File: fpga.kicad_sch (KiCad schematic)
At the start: 57 parts, among them J7 2X05, Q6 2N7002, U11 LIFCL-40-9BG256C, U17 SC18IS602BIPW, U18 W25Q32JVSSIQ, Y2 OSC40M-3.3_S5

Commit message: Created loclib
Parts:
- R58, R65: footprint antmicro-footprints:0603-res -> crosslink-nx-video-converter-footprints:0603-res; symbol antmicroResistors0603:R_0R_0603 -> crosslink-nx-video-converter:R_0R_0603
- U11: footprint antmicro-footprints:BGA-256_16x16_14.0x14.0mm -> crosslink-nx-video-converter-footprints:BGA-256_16x16_14.0x14.0mm; symbol antmicroBGAchips:LIFCL-40-9BG256C -> crosslink-nx-video-converter:LIFCL-40-9BG256C

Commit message: Added revision and title to the schematic sheets
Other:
- title: (none) -> CrossLink-NX Video Converter
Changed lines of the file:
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@@
 (kicad_sch (version 20211123) (generator eeschema)
   (paper "A3")
+  (title_block
+    (title "CrossLink-NX Video Converter")
+    (date "2022-10-27")
+    (rev "1.0.0")
+    (comment 1 "www.antmicro.com")
+    (comment 2 "Antmicro Ltd.")
+  )
   (junction (at 336.55 39.37) (diameter 0) (color 0 0 0 0)
   )

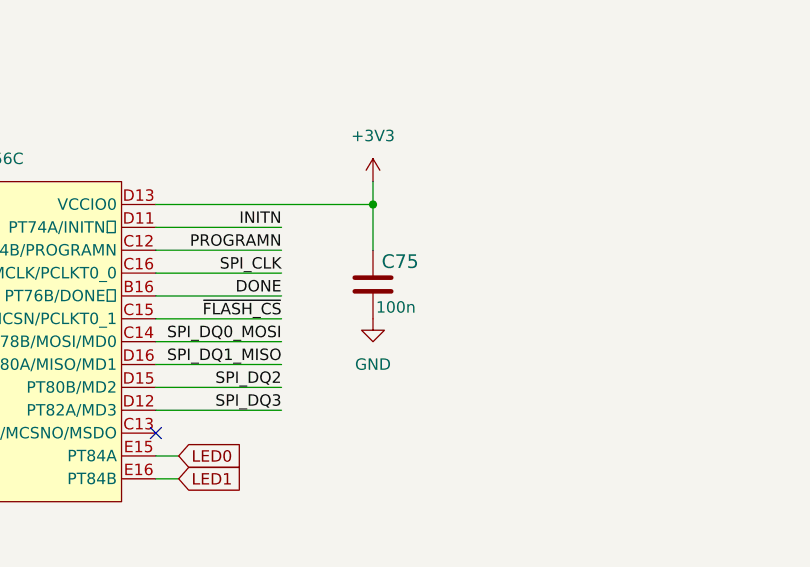
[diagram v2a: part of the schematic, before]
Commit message: Update PCB routing
- apply new DRC
- add FPGA package delay to the high speed traces tunning
- improve GND and power planes
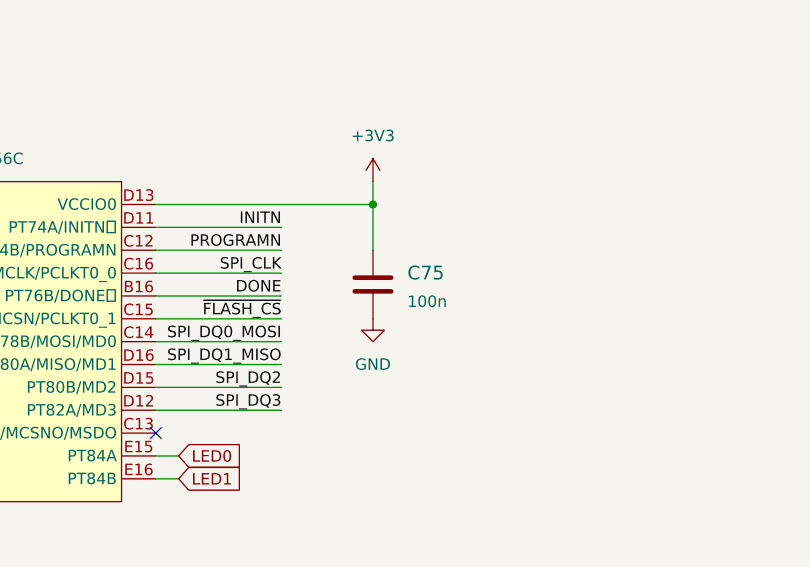
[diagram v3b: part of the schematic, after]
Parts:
- removed C75: C_100n_0402, crosslink-nx-video-converter-footprints:0402-cap, symbol crosslink-nx-video-converter:C_100n_0402
- added C75: C_100n_0201, crosslink-nx-video-converter-footprints:0201-res, symbol crosslink-nx-video-converter:C_100n_0201
- U11: footprint crosslink-nx-video-converter-footprints:BGA-256_16x16_14.0x14.0mm -> crosslink-nx-video-converter-footprints:CrosslinkNX-BGA-256_16x16_14.0x14.0mm
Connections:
- net +3V3: now also C75.1
- net GND: now also C75.2

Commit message: Update project naming convention
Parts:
- C75: footprint crosslink-nx-video-converter-footprints:0201-res -> sdi-mipi-cross-converter-footprints:0201-res; symbol crosslink-nx-video-converter:C_100n_0201 -> sdi-mipi-cross-converter:C_100n_0201
- C79, C80, C81, C82: footprint crosslink-nx-video-converter-footprints:0402-cap -> sdi-mipi-cross-converter-footprints:0402-cap; symbol crosslink-nx-video-converter:C_100n_0402 -> sdi-mipi-cross-converter:C_100n_0402
- D5: footprint crosslink-nx-video-converter-footprints:LED_0603 -> sdi-mipi-cross-converter-footprints:LED_0603; symbol crosslink-nx-video-converter:LTST-C190GKT -> sdi-mipi-cross-converter:LTST-C190GKT
- D6: footprint crosslink-nx-video-converter-footprints:LED_0603 -> sdi-mipi-cross-converter-footprints:LED_0603; symbol crosslink-nx-video-converter:LTST-C190KRKT -> sdi-mipi-cross-converter:LTST-C190KRKT
- J7: footprint crosslink-nx-video-converter-footprints:SHF-105-01-X-D-SM -> sdi-mipi-cross-converter-footprints:SHF-105-01-X-D-SM; symbol crosslink-nx-video-converter:2X05 -> sdi-mipi-cross-converter:2X05
- Q6: footprint crosslink-nx-video-converter-footprints:SOT-23-3 -> sdi-mipi-cross-converter-footprints:SOT-23-3; symbol crosslink-nx-video-converter:2N7002 -> sdi-mipi-cross-converter:2N7002
- R131, R132, R39, R66, R67, R69, R71, R75, R76, R77, R78, R80, R82, R85, R86, R88, R92, R94, R95, R96: footprint crosslink-nx-video-converter-footprints:0402-res -> sdi-mipi-cross-converter-footprints:0402-res; symbol crosslink-nx-video-converter:R_0R_0402 -> sdi-mipi-cross-converter:R_0R_0402
- R58, R65: footprint crosslink-nx-video-converter-footprints:0603-res -> sdi-mipi-cross-converter-footprints:0603-res; symbol crosslink-nx-video-converter:R_0R_0603 -> sdi-mipi-cross-converter:R_0R_0603
- R68, R81, R91, R97: footprint crosslink-nx-video-converter-footprints:0402-res -> sdi-mipi-cross-converter-footprints:0402-res; symbol crosslink-nx-video-converter:R_10k_0402 -> sdi-mipi-cross-converter:R_10k_0402
- R70, R72, R84: footprint crosslink-nx-video-converter-footprints:0402-res -> sdi-mipi-cross-converter-footprints:0402-res; symbol crosslink-nx-video-converter:R_100R_0402 -> sdi-mipi-cross-converter:R_100R_0402
- R79: footprint crosslink-nx-video-converter-footprints:0402-res -> sdi-mipi-cross-converter-footprints:0402-res; symbol crosslink-nx-video-converter:R_1k_0402 -> sdi-mipi-cross-converter:R_1k_0402
- R83, R87, R90: footprint crosslink-nx-video-converter-footprints:0402-res -> sdi-mipi-cross-converter-footprints:0402-res; symbol crosslink-nx-video-converter:R_4k7_0402 -> sdi-mipi-cross-converter:R_4k7_0402
- R89, R93: footprint crosslink-nx-video-converter-footprints:0402-res -> sdi-mipi-cross-converter-footprints:0402-res; symbol crosslink-nx-video-converter:R_2k2_0402 -> sdi-mipi-cross-converter:R_2k2_0402
- S1: footprint crosslink-nx-video-converter-footprints:B3U-3000P -> sdi-mipi-cross-converter-footprints:B3U-3000P; symbol crosslink-nx-video-converter:B3U-3000PM -> sdi-mipi-cross-converter:B3U-3000PM
- TP15, TP16, TP17, TP18, TP19, TP20, TP21, TP22: footprint crosslink-nx-video-converter-footprints:Testpoint_smd_0_75mm -> sdi-mipi-cross-converter-footprints:Testpoint_smd_0_75mm; symbol crosslink-nx-video-converter:TP_SMD_0_75MM -> sdi-mipi-cross-converter:TP_SMD_0_75MM
- U11: footprint crosslink-nx-video-converter-footprints:CrosslinkNX-BGA-256_16x16_14.0x14.0mm -> sdi-mipi-cross-converter-footprints:CrosslinkNX-BGA-256_16x16_14.0x14.0mm; symbol crosslink-nx-video-converter:LIFCL-40-9BG256C -> sdi-mipi-cross-converter:LIFCL-40-9BG256C
- U17: footprint crosslink-nx-video-converter-footprints:SC18IS602B -> sdi-mipi-cross-converter-footprints:SC18IS602B; symbol crosslink-nx-video-converter:SC18IS602BIPW -> sdi-mipi-cross-converter:SC18IS602BIPW
- U18: footprint crosslink-nx-video-converter-footprints:SOIC-8_W5.3mm -> sdi-mipi-cross-converter-footprints:SOIC-8_W5.3mm; symbol crosslink-nx-video-converter:W25Q32JVSSIQ -> sdi-mipi-cross-converter:W25Q32JVSSIQ
- Y2: footprint crosslink-nx-video-converter-footprints:OSC-4_5.0x3.2mm -> sdi-mipi-cross-converter-footprints:OSC-4_5.0x3.2mm; symbol crosslink-nx-video-converter:OSC40M-3.3_S5 -> sdi-mipi-cross-converter:OSC40M-3.3_S5

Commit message: Bump to 1.1.0, update naming
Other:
- title: CrossLink-NX Video Converter -> SDI-MIPI Cross Converter

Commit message: Update U11/LIFCL-40-9BG256C footprint property
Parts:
- U11: footprint sdi-mipi-cross-converter-footprints:CrosslinkNX-BGA-256_16x16_14.0x14.0mm -> sdi-mipi-cross-converter-footprints:BGA-256_16x16_14.0x14.0mm
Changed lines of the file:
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@@
     (property "Reference" "U11" (id 0) (at 74.295 123.19 0))
     (property "Value" "LIFCL-40-9BG256C" (id 1) (at 74.295 125.73 0))
-    (property "Footprint" "sdi-mipi-cross-converter-footprints:CrosslinkNX-BGA-256_16x16_14.0x14.0mm" (id 2) (at 76.835 282.575 0)
+    (property "Footprint" "sdi-mipi-cross-converter-footprints:BGA-256_16x16_14.0x14.0mm" (id 2) (at 76.835 282.575 0)
       (effects (font (size 1.27 1.27)) hide)
     )
@@
     (property "Reference" "U11" (id 0) (at 123.825 120.65 0))
     (property "Value" "LIFCL-40-9BG256C" (id 1) (at 123.825 123.19 0))
-    (property "Footprint" "sdi-mipi-cross-converter-footprints:CrosslinkNX-BGA-256_16x16_14.0x14.0mm" (id 2) (at 126.365 282.575 0)
+    (property "Footprint" "sdi-mipi-cross-converter-footprints:BGA-256_16x16_14.0x14.0mm" (id 2) (at 126.365 282.575 0)
       (effects (font (size 1.27 1.27)) hide)
     )
@@
     (property "Reference" "U11" (id 0) (at 95.25 45.72 0))
     (property "Value" "LIFCL-40-9BG256C" (id 1) (at 95.25 48.26 0))
-    (property "Footprint" "sdi-mipi-cross-converter-footprints:CrosslinkNX-BGA-256_16x16_14.0x14.0mm" (id 2) (at 97.155 211.455 0)
-      (effects (font (size 1.27 1.27)) hide)
-    )
+    (property "Footprint" "sdi-mipi-cross-converter-footprints:BGA-256_16x16_14.0x14.0mm" (id 2) (at 97.155 211.455 0)
+      (effects (font (size 1.27 1.27)) hide)
+    )

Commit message: Update naming convention
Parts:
- C75: footprint sdi-mipi-cross-converter-footprints:0201-res -> sdi-mipi-video-converter-footprints:0201-res; symbol sdi-mipi-cross-converter:C_100n_0201 -> sdi-mipi-video-converter:C_100n_0201
- C79, C80, C81, C82: footprint sdi-mipi-cross-converter-footprints:0402-cap -> sdi-mipi-video-converter-footprints:0402-cap; symbol sdi-mipi-cross-converter:C_100n_0402 -> sdi-mipi-video-converter:C_100n_0402
- D5: footprint sdi-mipi-cross-converter-footprints:LED_0603 -> sdi-mipi-video-converter-footprints:LED_0603; symbol sdi-mipi-cross-converter:LTST-C190GKT -> sdi-mipi-video-converter:LTST-C190GKT
- D6: footprint sdi-mipi-cross-converter-footprints:LED_0603 -> sdi-mipi-video-converter-footprints:LED_0603; symbol sdi-mipi-cross-converter:LTST-C190KRKT -> sdi-mipi-video-converter:LTST-C190KRKT
- J7: footprint sdi-mipi-cross-converter-footprints:SHF-105-01-X-D-SM -> sdi-mipi-video-converter-footprints:SHF-105-01-X-D-SM; symbol sdi-mipi-cross-converter:2X05 -> sdi-mipi-video-converter:2X05
- Q6: footprint sdi-mipi-cross-converter-footprints:SOT-23-3 -> sdi-mipi-video-converter-footprints:SOT-23-3; symbol sdi-mipi-cross-converter:2N7002 -> sdi-mipi-video-converter:2N7002
- R131, R132, R39, R66, R67, R69, R71, R75, R76, R77, R78, R80, R82, R85, R86, R88, R92, R94, R95, R96: footprint sdi-mipi-cross-converter-footprints:0402-res -> sdi-mipi-video-converter-footprints:0402-res; symbol sdi-mipi-cross-converter:R_0R_0402 -> sdi-mipi-video-converter:R_0R_0402
- R58, R65: footprint sdi-mipi-cross-converter-footprints:0603-res -> sdi-mipi-video-converter-footprints:0603-res; symbol sdi-mipi-cross-converter:R_0R_0603 -> sdi-mipi-video-converter:R_0R_0603
- R68, R81, R91, R97: footprint sdi-mipi-cross-converter-footprints:0402-res -> sdi-mipi-video-converter-footprints:0402-res; symbol sdi-mipi-cross-converter:R_10k_0402 -> sdi-mipi-video-converter:R_10k_0402
- R70, R72, R84: footprint sdi-mipi-cross-converter-footprints:0402-res -> sdi-mipi-video-converter-footprints:0402-res; symbol sdi-mipi-cross-converter:R_100R_0402 -> sdi-mipi-video-converter:R_100R_0402
- R79: footprint sdi-mipi-cross-converter-footprints:0402-res -> sdi-mipi-video-converter-footprints:0402-res; symbol sdi-mipi-cross-converter:R_1k_0402 -> sdi-mipi-video-converter:R_1k_0402
- R83, R87, R90: footprint sdi-mipi-cross-converter-footprints:0402-res -> sdi-mipi-video-converter-footprints:0402-res; symbol sdi-mipi-cross-converter:R_4k7_0402 -> sdi-mipi-video-converter:R_4k7_0402
- R89, R93: footprint sdi-mipi-cross-converter-footprints:0402-res -> sdi-mipi-video-converter-footprints:0402-res; symbol sdi-mipi-cross-converter:R_2k2_0402 -> sdi-mipi-video-converter:R_2k2_0402
- S1: footprint sdi-mipi-cross-converter-footprints:B3U-3000P -> sdi-mipi-video-converter-footprints:B3U-3000P; symbol sdi-mipi-cross-converter:B3U-3000PM -> sdi-mipi-video-converter:B3U-3000PM
- TP15, TP16, TP17, TP18, TP19, TP20, TP21, TP22: footprint sdi-mipi-cross-converter-footprints:Testpoint_smd_0_75mm -> sdi-mipi-video-converter-footprints:Testpoint_smd_0_75mm; symbol sdi-mipi-cross-converter:TP_SMD_0_75MM -> sdi-mipi-video-converter:TP_SMD_0_75MM
- U11: footprint sdi-mipi-cross-converter-footprints:BGA-256_16x16_14.0x14.0mm -> sdi-mipi-video-converter-footprints:BGA-256_16x16_14.0x14.0mm; symbol sdi-mipi-cross-converter:LIFCL-40-9BG256C -> sdi-mipi-video-converter:LIFCL-40-9BG256C
- U17: footprint sdi-mipi-cross-converter-footprints:SC18IS602B -> sdi-mipi-video-converter-footprints:SC18IS602B; symbol sdi-mipi-cross-converter:SC18IS602BIPW -> sdi-mipi-video-converter:SC18IS602BIPW
- U18: footprint sdi-mipi-cross-converter-footprints:SOIC-8_W5.3mm -> sdi-mipi-video-converter-footprints:SOIC-8_W5.3mm; symbol sdi-mipi-cross-converter:W25Q32JVSSIQ -> sdi-mipi-video-converter:W25Q32JVSSIQ
- Y2: footprint sdi-mipi-cross-converter-footprints:OSC-4_5.0x3.2mm -> sdi-mipi-video-converter-footprints:OSC-4_5.0x3.2mm; symbol sdi-mipi-cross-converter:OSC40M-3.3_S5 -> sdi-mipi-video-converter:OSC40M-3.3_S5
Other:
- title: SDI-MIPI Cross Converter -> SDI-MIPI Video Converter
